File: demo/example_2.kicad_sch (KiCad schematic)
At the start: 12 parts

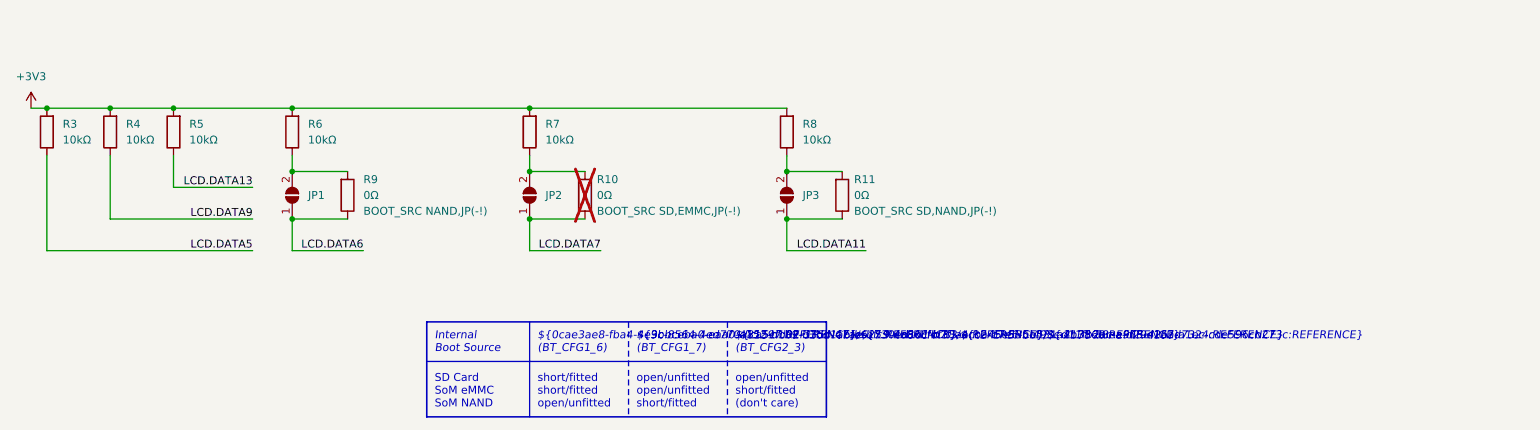
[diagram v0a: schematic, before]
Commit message: Update demo project for upcoming changes
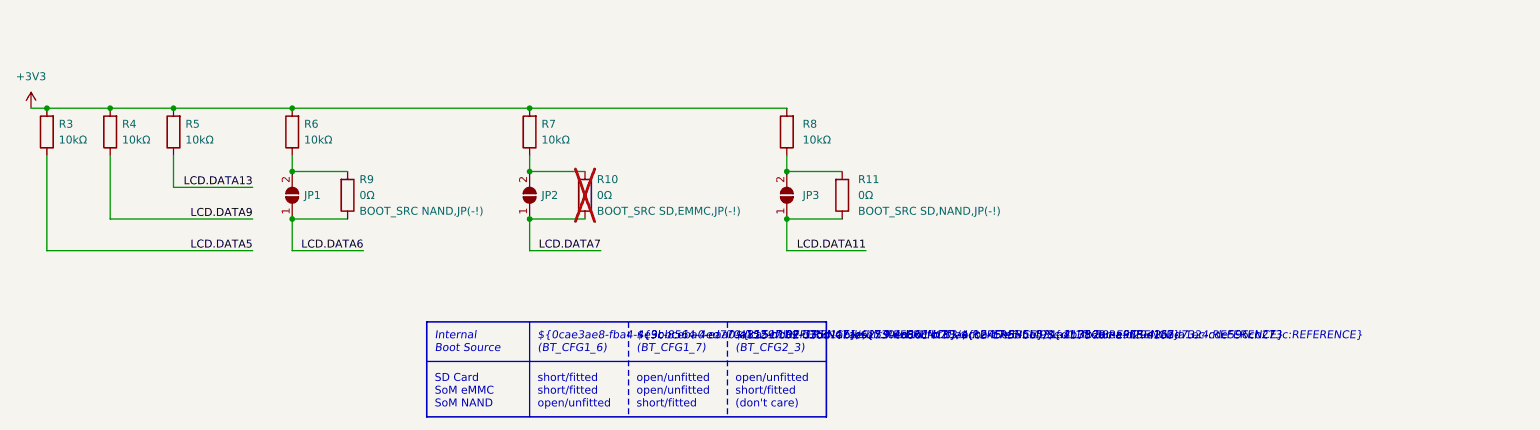
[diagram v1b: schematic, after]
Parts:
- R10: KiVar.Rule BOOT_SRC SD,EMMC,JP(-!) -> (none); Var (none) -> BOOT_SRC SD,EMMC,JP(-!)
- R11: KiVar.Rule BOOT_SRC SD,NAND,JP(-!) -> (none); Var (none) -> BOOT_SRC SD,NAND,JP(-!)
- R9: KiVar.Rule BOOT_SRC NAND,JP(-!) -> (none); Var (none) -> BOOT_SRC NAND,JP(-!)
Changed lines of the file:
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@@
 	(title_block
 		(title "KiVar Demo")
-		(date "2024-03-18")
+		(date "2024-03-19")
 		(company "Author: Mark Hämmerling <dev@markh.de>")
 		(comment 1 "https://github.com/markh-de/KiVar")
@@
 		(fields_autoplaced yes)
 		(property "Reference" "JP1"
-			(at 123.825 92.7099 90)
+			(at 123.19 92.7099 90)
 			(effects
 				(font
@@
 		(fields_autoplaced yes)
 		(property "Reference" "JP2"
-			(at 161.925 92.7099 90)
+			(at 161.29 92.7099 90)
 			(effects
 				(font
@@
 		(on_board yes)
 		(dnp no)
+		(fields_autoplaced yes)
 		(property "Reference" "R9"
-			(at 132.715 90.1699 0)
+			(at 132.08 90.1699 0)
 			(effects
 				(font
@@
 		)
 		(property "Value" "0Ω"
-			(at 132.715 92.7099 0)
+			(at 132.08 92.7099 0)
 			(effects
 				(font
@@
 			)
 		)
-		(property "KiVar.Rule" "BOOT_SRC NAND,JP(-!)"
-			(at 132.715 95.2499 0)
+		(property "Var" "BOOT_SRC NAND,JP(-!)"
+			(at 132.08 95.2499 0)
 			(effects
 				(font
@@
 		(on_board yes)
 		(dnp no)
+		(fields_autoplaced yes)
 		(property "Reference" "R3"
-			(at 84.455 81.2799 0)
+			(at 83.82 81.2799 0)
 			(effects
 				(font
@@
 		)
 		(property "Value" "10kΩ"
-			(at 84.455 83.82 0)
+			(at 83.82 83.8199 0)
 			(effects
 				(font
@@
 		(on_board yes)
 		(dnp no)
+		(fields_autoplaced yes)
 		(property "Reference" "R7"
-			(at 161.925 81.2799 0)
+			(at 161.29 81.2799 0)
 			(effects
 				(font
@@
 		)
 		(property "Value" "10kΩ"
-			(at 161.925 83.82 0)
+			(at 161.29 83.8199 0)
 			(effects
 				(font
@@
 		(on_board yes)
 		(dnp no)
+		(fields_autoplaced yes)
 		(property "Reference" "R6"
-			(at 123.825 81.2799 0)
+			(at 123.19 81.2799 0)
 			(effects
 				(font
@@
 		)
 		(property "Value" "10kΩ"
-			(at 123.825 83.82 0)
+			(at 123.19 83.8199 0)
 			(effects
 				(font
@@
 		(on_board yes)
 		(dnp no)
+		(fields_autoplaced yes)
 		(property "Reference" "R5"
-			(at 104.775 81.2799 0)
+			(at 104.14 81.2799 0)
 			(effects
 				(font
@@
 		)
 		(property "Value" "10kΩ"
-			(at 104.775 83.82 0)
+			(at 104.14 83.8199 0)
 			(effects
 				(font
@@
 			)
 		)
-		(property "KiVar.Rule" "BOOT_SRC SD,EMMC,JP(-!)"
+		(property "Var" "BOOT_SRC SD,EMMC,JP(-!)"
 			(at 170.18 95.2499 0)
 			(effects
@@
 		(fields_autoplaced yes)
 		(property "Reference" "R11"
-			(at 211.455 90.1699 0)
+			(at 212.09 90.1699 0)
 			(effects
 				(font
@@
 		)
 		(property "Value" "0Ω"
-			(at 211.455 92.7099 0)
+			(at 212.09 92.7099 0)
 			(effects
 				(font
@@
 			)
 		)
-		(property "KiVar.Rule" "BOOT_SRC SD,NAND,JP(-!)"
-			(at 211.455 95.2499 0)
+		(property "Var" "BOOT_SRC SD,NAND,JP(-!)"
+			(at 212.09 95.2499 0)
 			(effects
 				(font
@@
 		(on_board yes)
 		(dnp no)
+		(fields_autoplaced yes)
 		(property "Reference" "R4"
-			(at 94.615 81.2799 0)
+			(at 93.98 81.2799 0)
 			(effects
 				(font
@@
 		)
 		(property "Value" "10kΩ"
-			(at 94.615 83.82 0)
+			(at 93.98 83.8199 0)
 			(effects
 				(font
@@
 		(on_board yes)
 		(dnp no)
+		(fields_autoplaced yes)
 		(property "Reference" "R8"
 			(at 203.2 81.2799 0)
@@
 		)
 		(property "Value" "10kΩ"
-			(at 203.2 83.82 0)
-			(effects
-				(font
+			(at 203.2 83.8199 0)
+			(effects
+				(font

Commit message: Make use of new 0.2.0 features in demo project, use different expression types
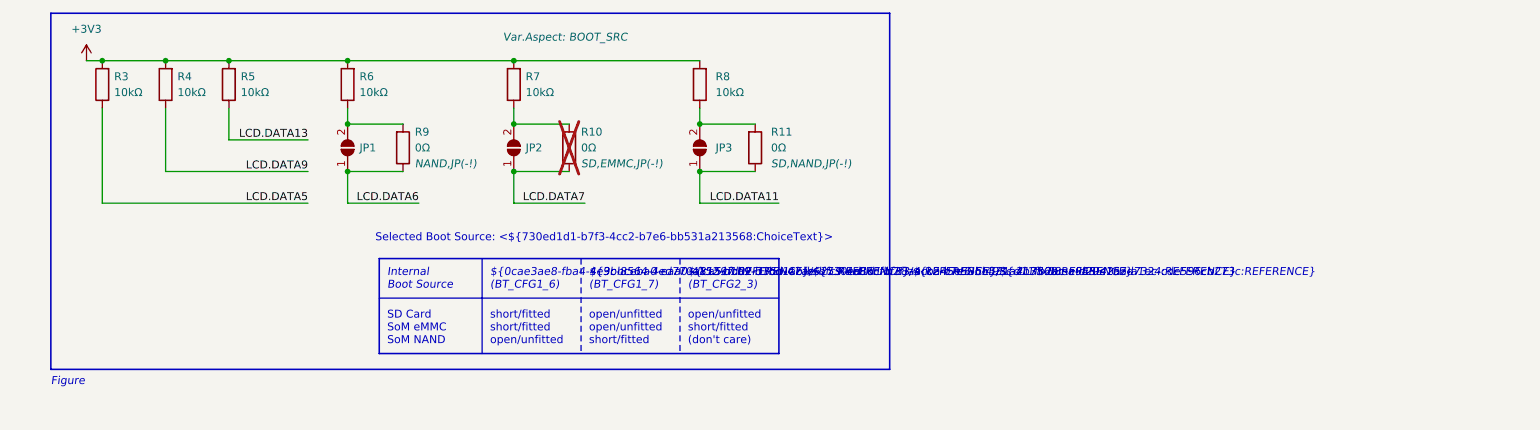
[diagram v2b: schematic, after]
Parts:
- R10: Var BOOT_SRC SD,EMMC,JP(-!) -> SD,EMMC,JP(-!); Var.Aspect (none) -> BOOT_SRC
- R11: Var BOOT_SRC SD,NAND,JP(-!) -> SD,NAND,JP(-!); Var.Aspect (none) -> BOOT_SRC
- R9: ChoiceText (none) -> SoM eMMC; ChoiceText.Var (none) -> SD(SD Card) EMMC(SoM eMMC) NAND(SoM NAND) JP(Manual); Var BOOT_SRC NAND,JP(-!) -> NAND,JP(-!); Var.Aspect (none) -> BOOT_SRC
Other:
- note added: "Figure"
- note added: "Selected Boot Source: <${730ed1d1-b7f3-4cc2-b7e6-bb531a213568:ChoiceText}>"
- moved on the sheet: JP1, JP2, JP3, R10, R11, R3, R4, R5, R6, R7, R8, R9
